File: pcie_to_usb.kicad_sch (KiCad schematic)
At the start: 88 parts, among them J14 USB-A_Samtec_USB-A-S-F-B-VT_V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, J8 USB-A_Samtec_USB-A-S-F-B-VT_V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, U2 UPD720202K8-711-BAA-A, U3 AP22615A_TSOT26, U4 AP22615A_TSOT26, U5 W25Q80DV_USON, Y1 Resonator_24MHz_ECX-1247

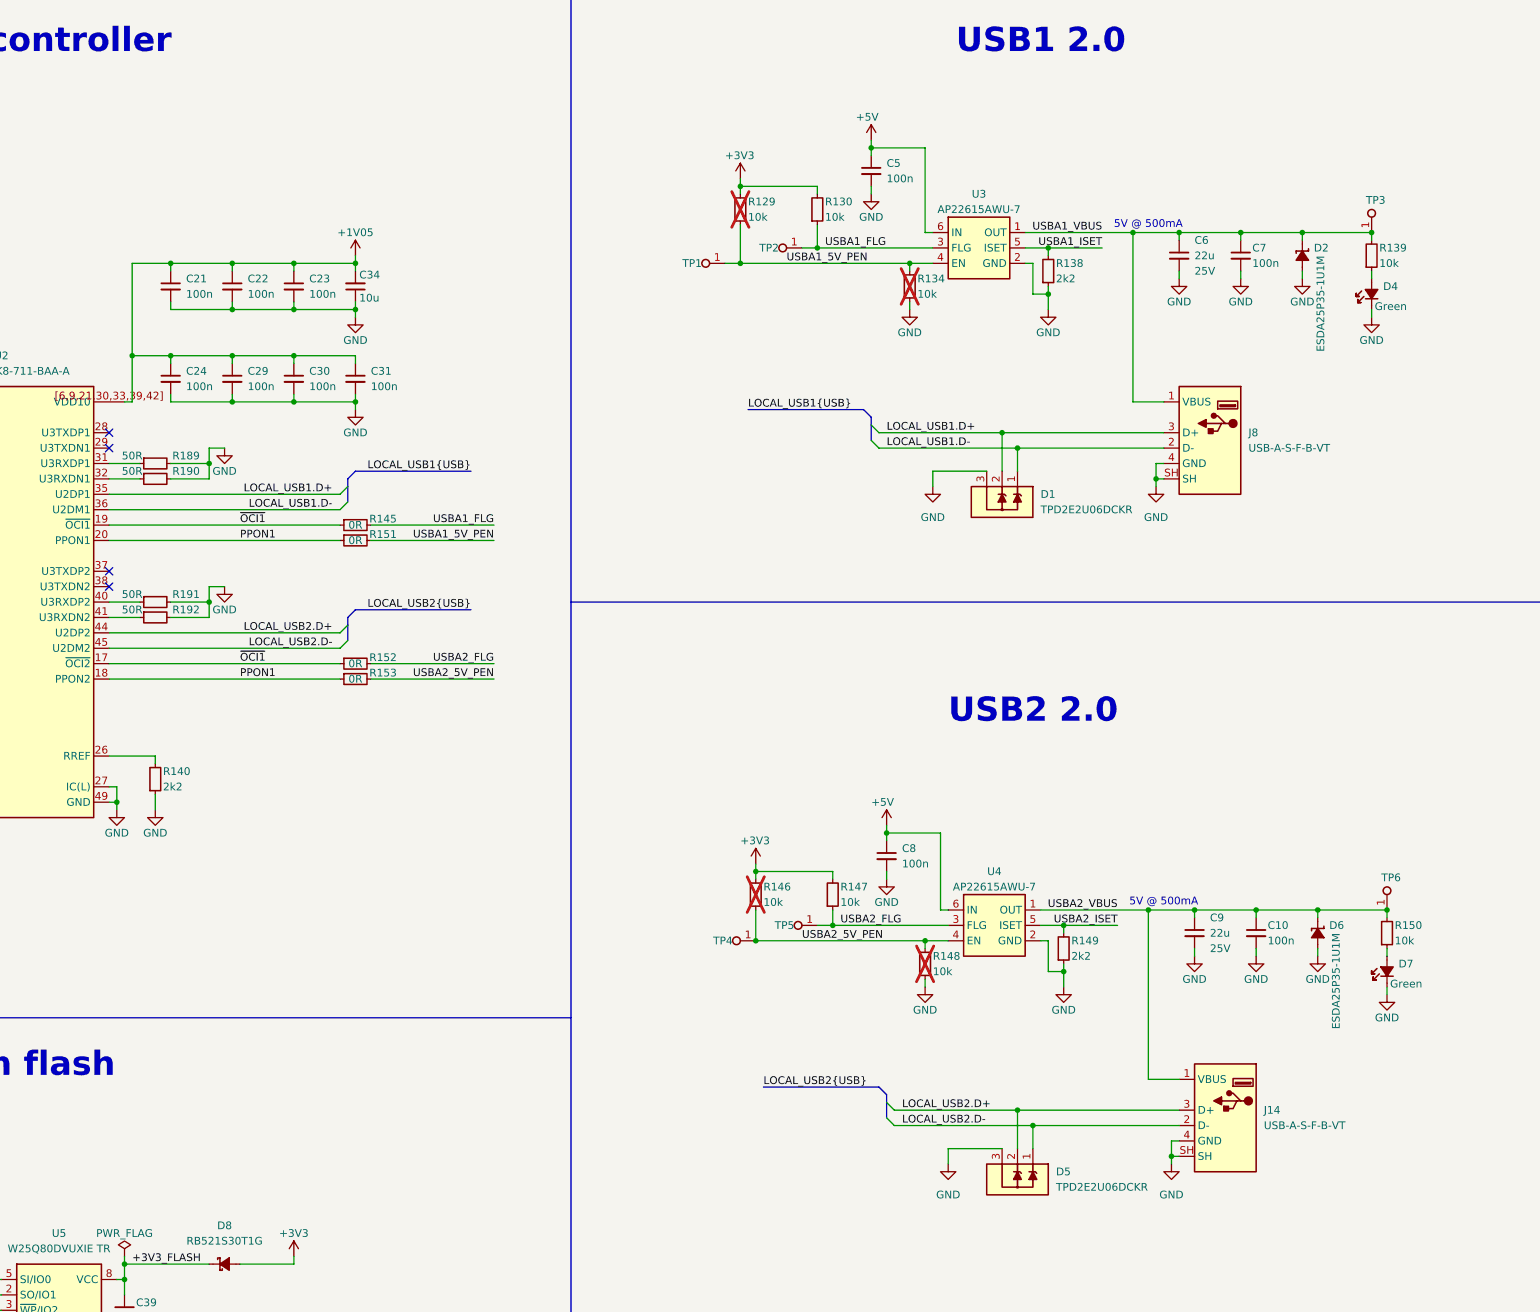
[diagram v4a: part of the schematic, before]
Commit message: [#100720] Change USB-A to USB on JST connector
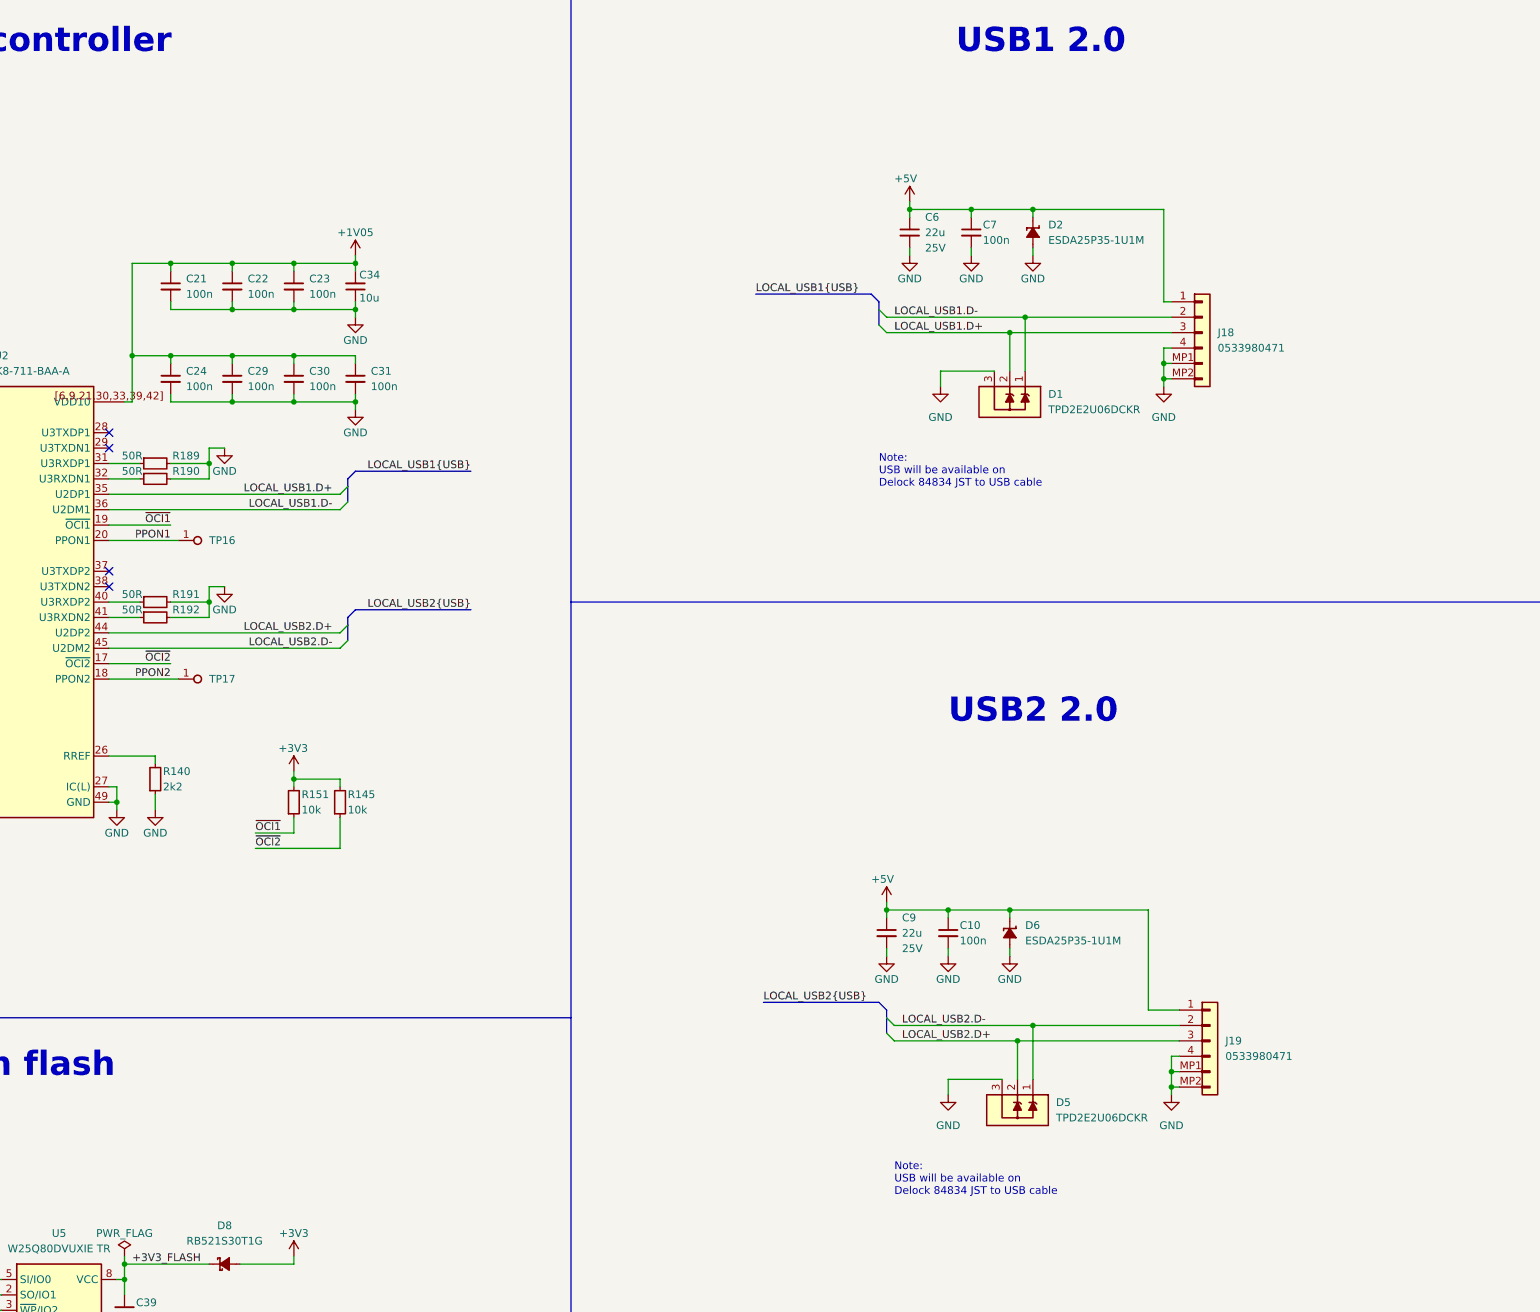
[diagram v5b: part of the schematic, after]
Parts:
- removed C5, C8: C_100n_0402, antmicro-footprints:C_0402_1005Metric, symbol antmicroCapacitors0402:C_100n_0402
- removed D4, D7: LED_G_0603_LTST-C190GKT, antmicro-footprints:LED_0603_1608Metric_G, symbol antmicroLEDIndicationDiscrete:LED_G_0603_LTST-C190GKT
- removed J14, J8: USB-A_Samtec_USB-A-S-F-B-VT_Vertical, antmicro-footprints:USB-A_Receptacle_Samtec_USB-A-S-F-B-VT, symbol antmicroUSBConnectors:USB-A_Samtec_USB-A-S-F-B-VT_Vertical
- removed R129, R130, R134, R139, R146, R147, R148, R150: R_10k_0402, antmicro-footprints:R_0402_1005Metric, symbol antmicroResistors0402:R_10k_0402
- removed R138, R149: R_2k2_0402, antmicro-footprints:R_0402_1005Metric, symbol antmicroResistors0402:R_2k2_0402
- removed R145, R151, R152, R153: R_0R_0402, antmicro-footprints:R_0402_1005Metric, symbol antmicroResistors0402:R_0R_0402
- removed TP1, TP2, TP3, TP4, TP5, TP6: TP_0.75mm_SMD, antmicro-footprints:TP_SMD_0.75mm, symbol antmicroTestPoints:TP_0.75mm_SMD
- removed U3, U4: AP22615A_TSOT26, antmicro-footprints:TSOT23-6, symbol antmicroPMICPowerDistributionSwitchesLoadDrivers:AP22615A_TSOT26
- added J18, J19: Molex_PicoBlade_1x4_0533980471, antmicro-footprints:Conn_Molex_PicoBlade_1x4_0533980471, symbol antmicroWire2BoardConnectors:Molex_PicoBlade_1x4_0533980471
- added R145, R151: R_10k_0402, antmicro-footprints:R_0402_1005Metric, symbol antmicroResistors0402:R_10k_0402
- added TP16, TP17: TP_0.75mm_SMD, antmicro-footprints:TP_SMD_0.75mm, symbol antmicroTestPoints:TP_0.75mm_SMD
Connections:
- net USBA1_VBUS is gone; now on net +5V: C6.1, C7.1, D2.1 (C)
- net USBA2_VBUS is gone; now on net +5V: C10.1, C9.1, D6.1 (C)
- net +3V3: now also R145.2, R151.2
- net +5V: now also J18.1, J19.1
- net GND: now also J18.4, J18.MP1, J18.MP2, J19.4, J19.MP1, J19.MP2
- net LOCAL_USB1.D+: now also J18.3
- net LOCAL_USB1.D-: now also J18.2
- net LOCAL_USB2.D+: now also J19.3
- net LOCAL_USB2.D-: now also J19.2
- net PPON1: now also TP16.1; no longer U2.18 (PPON2)
- net ~{OCI1}: now also R151.1; no longer U2.17 (~{OCI2})
- new net PPON2: TP17.1, U2.18 (PPON2)
- new net ~{OCI2}: R145.1, U2.17 (~{OCI2})
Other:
- note added: "Note: USB will be available on Delock 84834 JST to USB cable"
- note removed: "5V @ 500mA"
- moved on the sheet: C10, C6, C7, C9, D1, D2, D5, D6

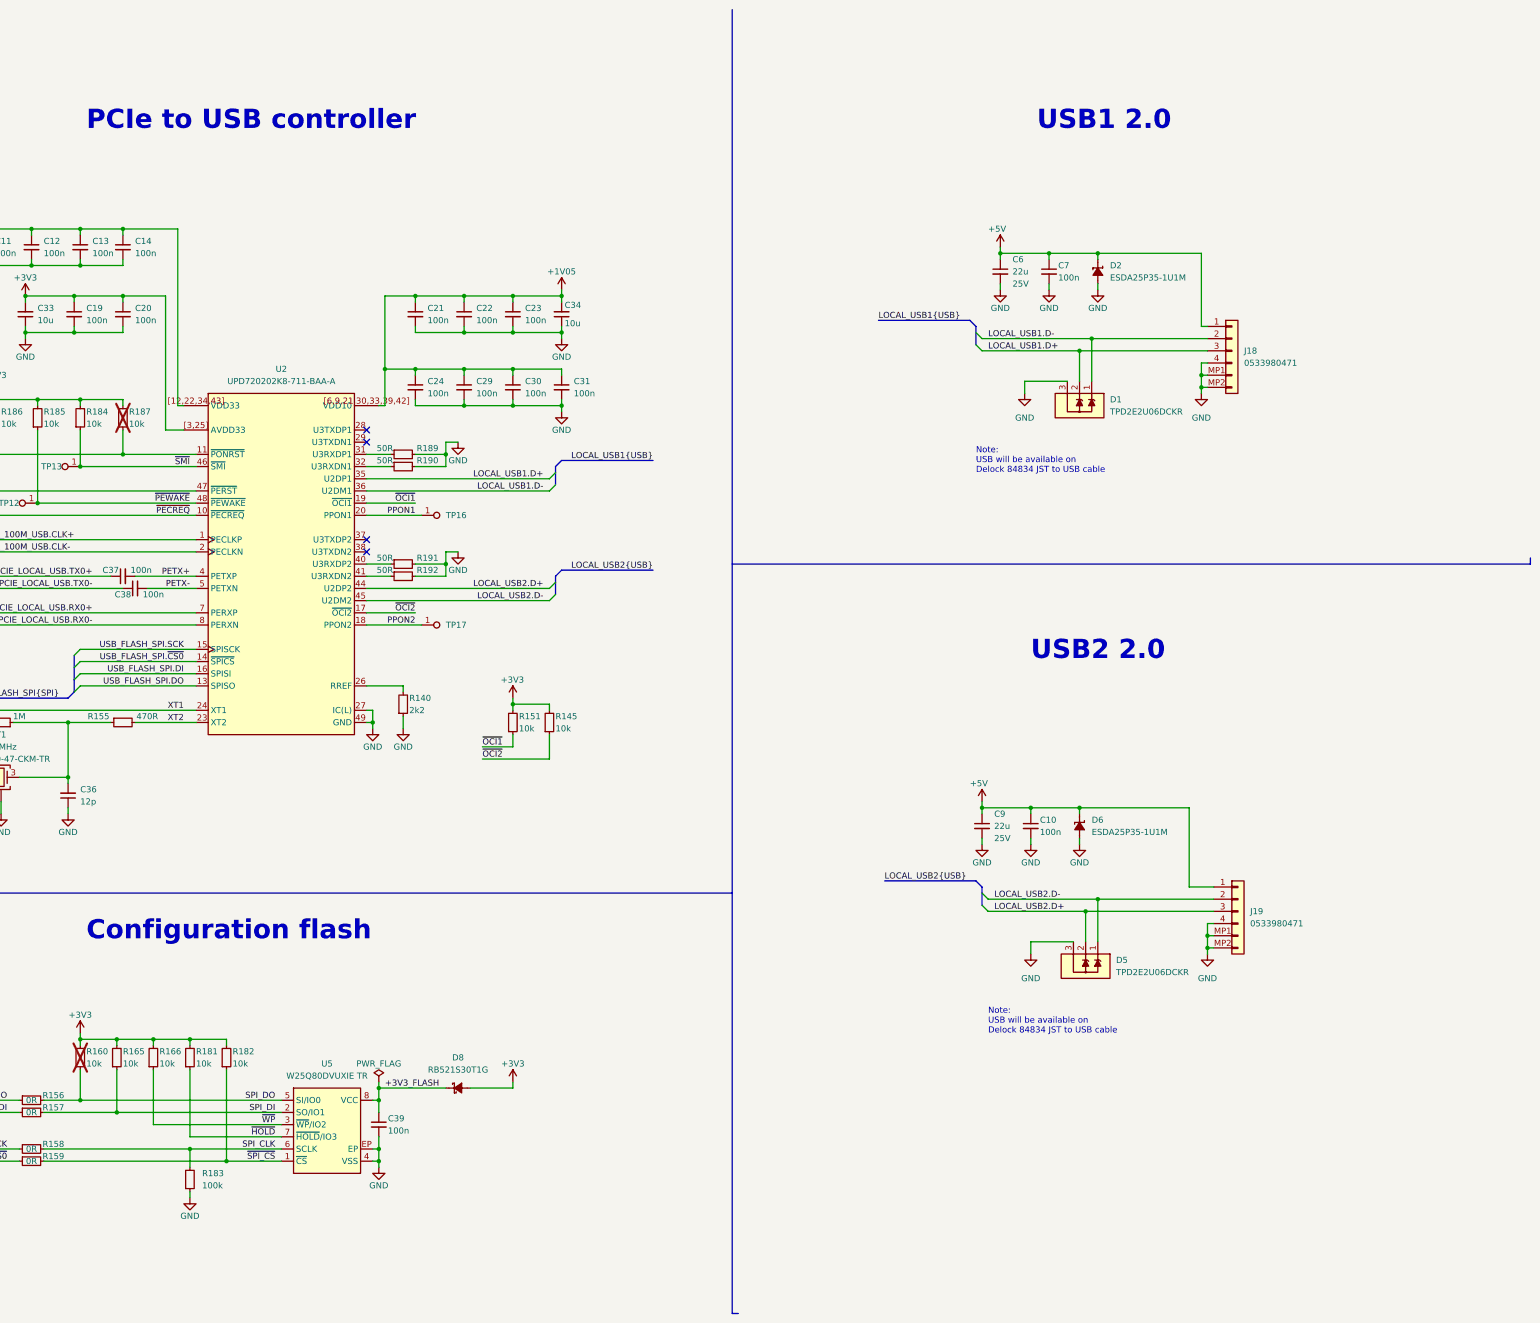
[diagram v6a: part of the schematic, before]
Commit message: [#100720] Add USB to PCIe controller Flash SPI Tag connect, add via stitching, clear DRC
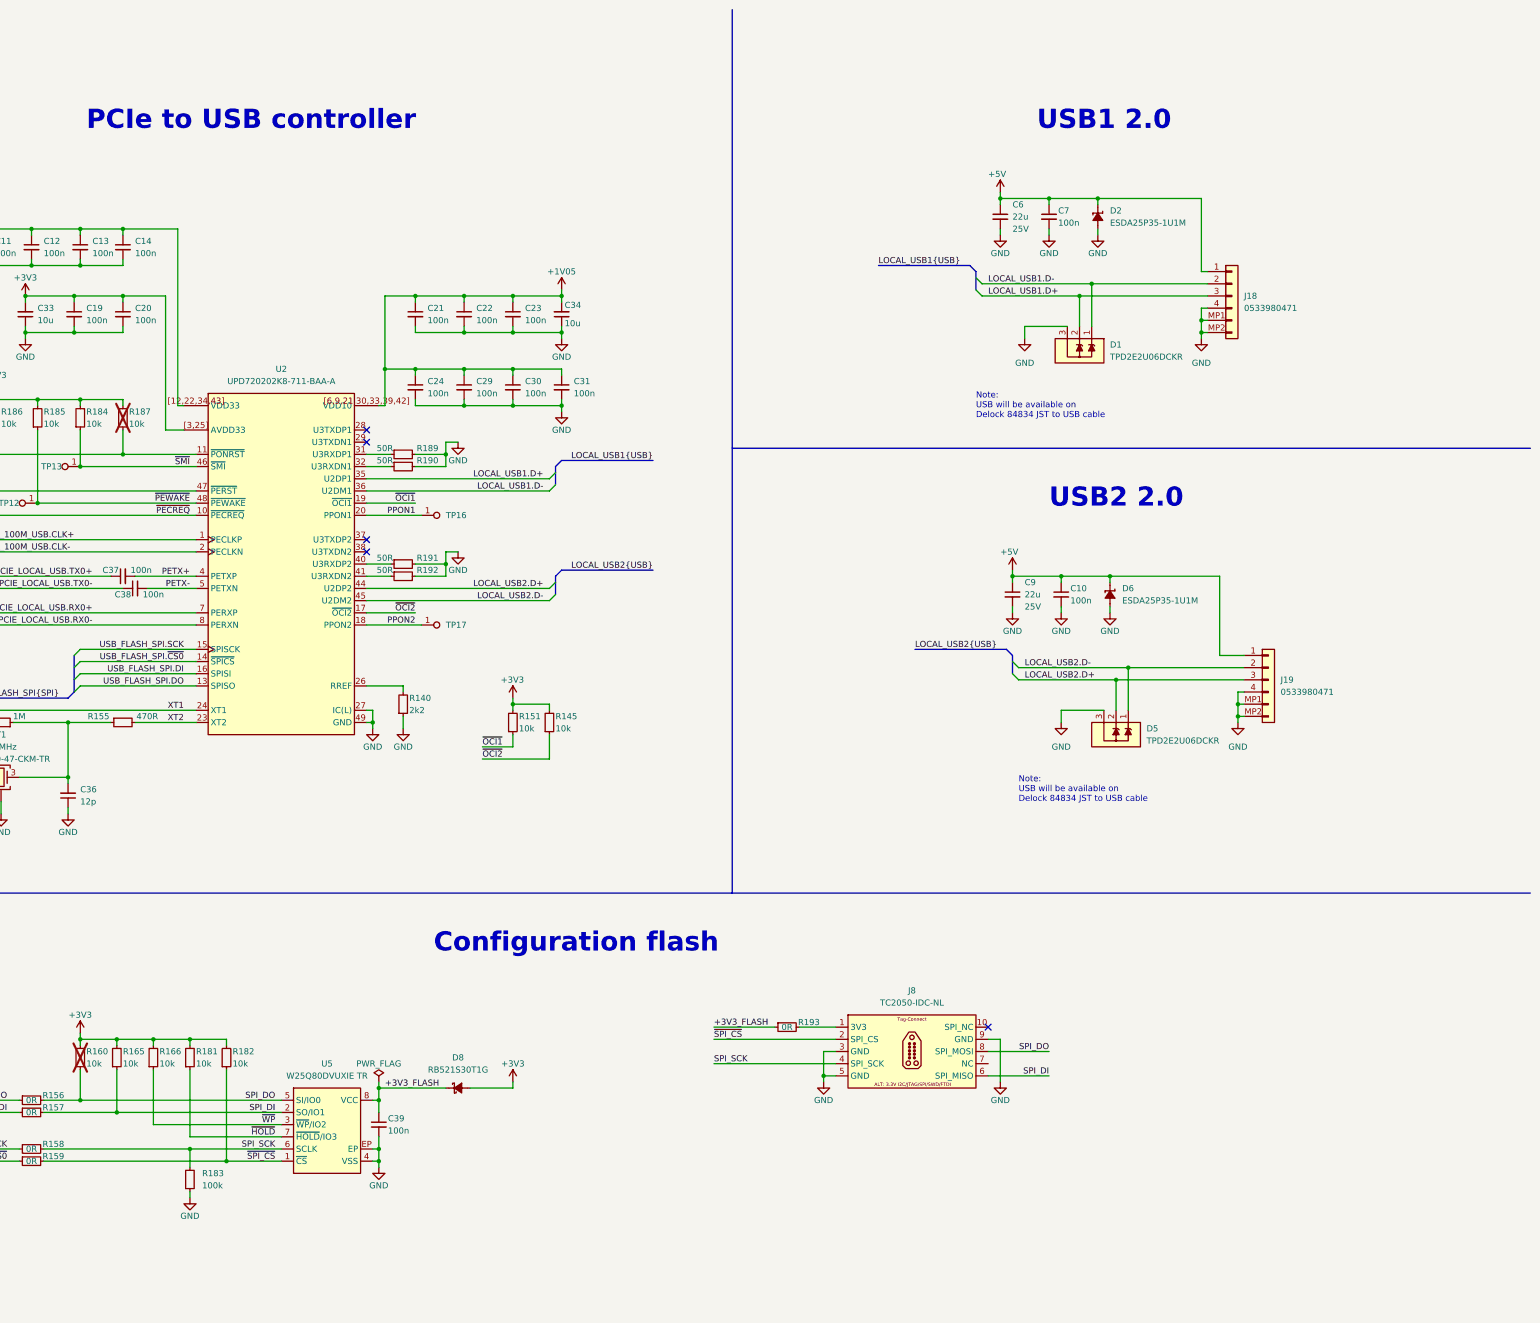
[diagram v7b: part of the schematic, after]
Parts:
- added J8: Tag-Connect_TC2050-IDC-NL_2x5_P1.27mm, antmicro-footprints:Tag-Connect_TC2050-IDC-NL_2x5_P1.27mm, symbol antmicroTestPoints:Tag-Connect_TC2050-IDC-NL_2x5_P1.27mm
- added R193: R_0R_0402, antmicro-footprints:R_0402_1005Metric, symbol antmicroResistors0402:R_0R_0402
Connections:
- net +3V3_FLASH: now also R193.1
- net GND: now also J8.3, J8.5, J8.9
- net SPI_DI: now also J8.6
- net SPI_DO: now also J8.8
- net ~{SPI_CS}: now also J8.2
- net SPI_CLK renamed SPI_SCK
- net SPI_SCK: now also J8.4
- new net: J8.1, R193.2
- no-connect marks 4 -> 5
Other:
- moved on the sheet: C10, C6, C7, C9, D1, D2, D5, D6, J18, J19

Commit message: [#100720] Add OR on USB D+/- lines
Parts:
- added R194, R195, R196, R197: R_0R_0402, antmicro-footprints:R_0402_1005Metric, symbol antmicroResistors0402:R_0R_0402
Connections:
- net LOCAL_USB1.D+: now also R195.2; no longer J18.3
- net LOCAL_USB1.D-: now also R194.2; no longer J18.2
- net LOCAL_USB2.D+: now also R197.2; no longer J19.3
- net LOCAL_USB2.D-: now also R196.2; no longer J19.2
- new net: J18.2, R194.1
- new net: J18.3, R195.1
- new net: J19.2, R196.1
- new net: J19.3, R197.1
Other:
- note added: "Note: Compatible cable: Delock 84834"
- note removed: "Note: USB will be available on Delock 84834 JST to USB cable"
